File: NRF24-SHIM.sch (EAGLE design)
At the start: 15 parts, among them M1 WIRELESS-NRF24L01, M2 WIRELESS-NRF24L01-PA-EXT

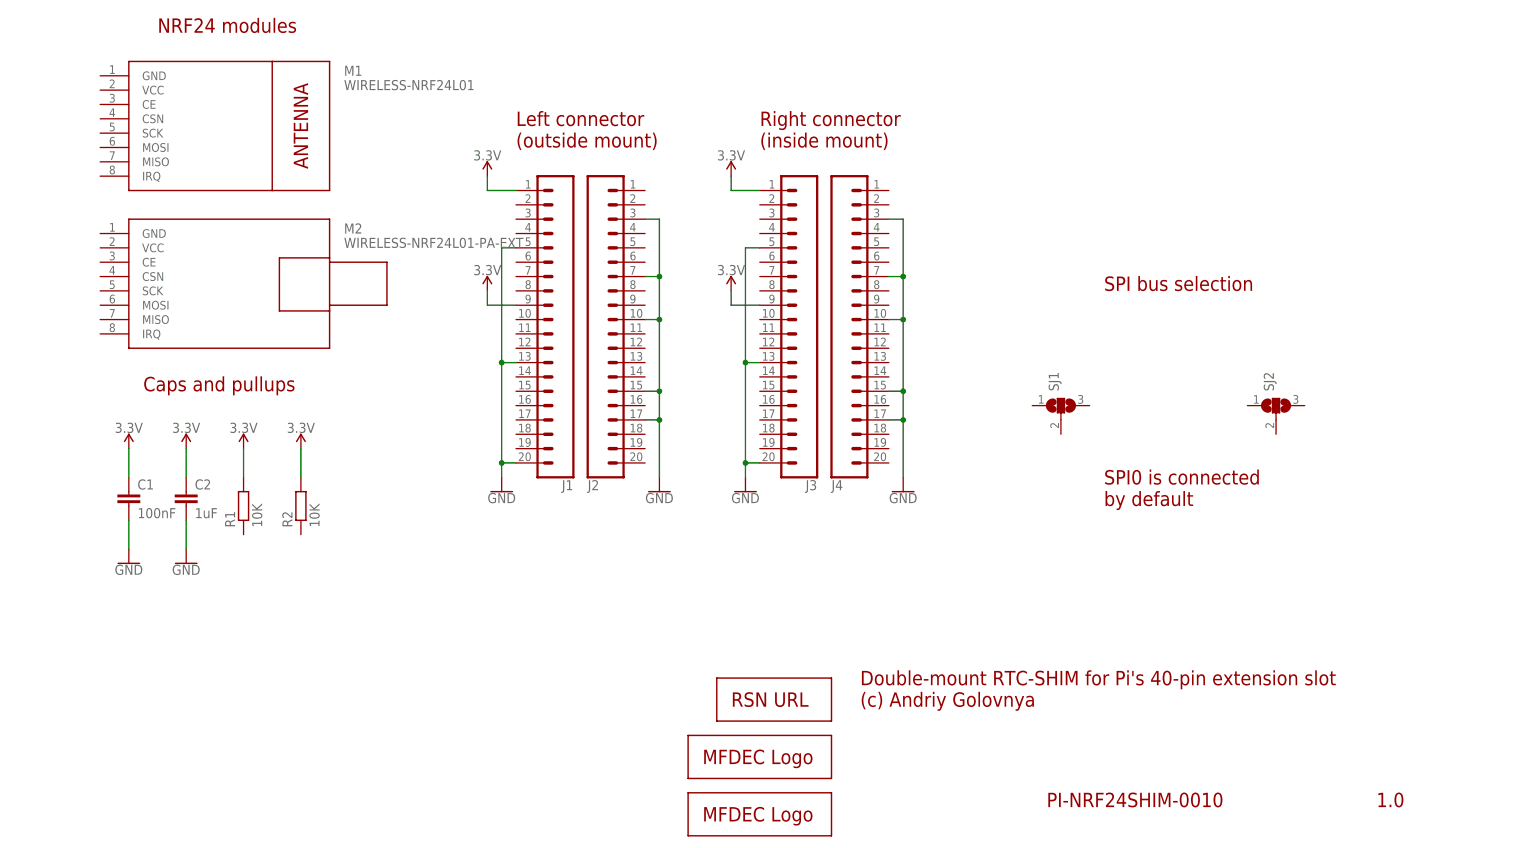
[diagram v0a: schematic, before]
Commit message: Add more pullups. Add more solder joints. Did some tracing.
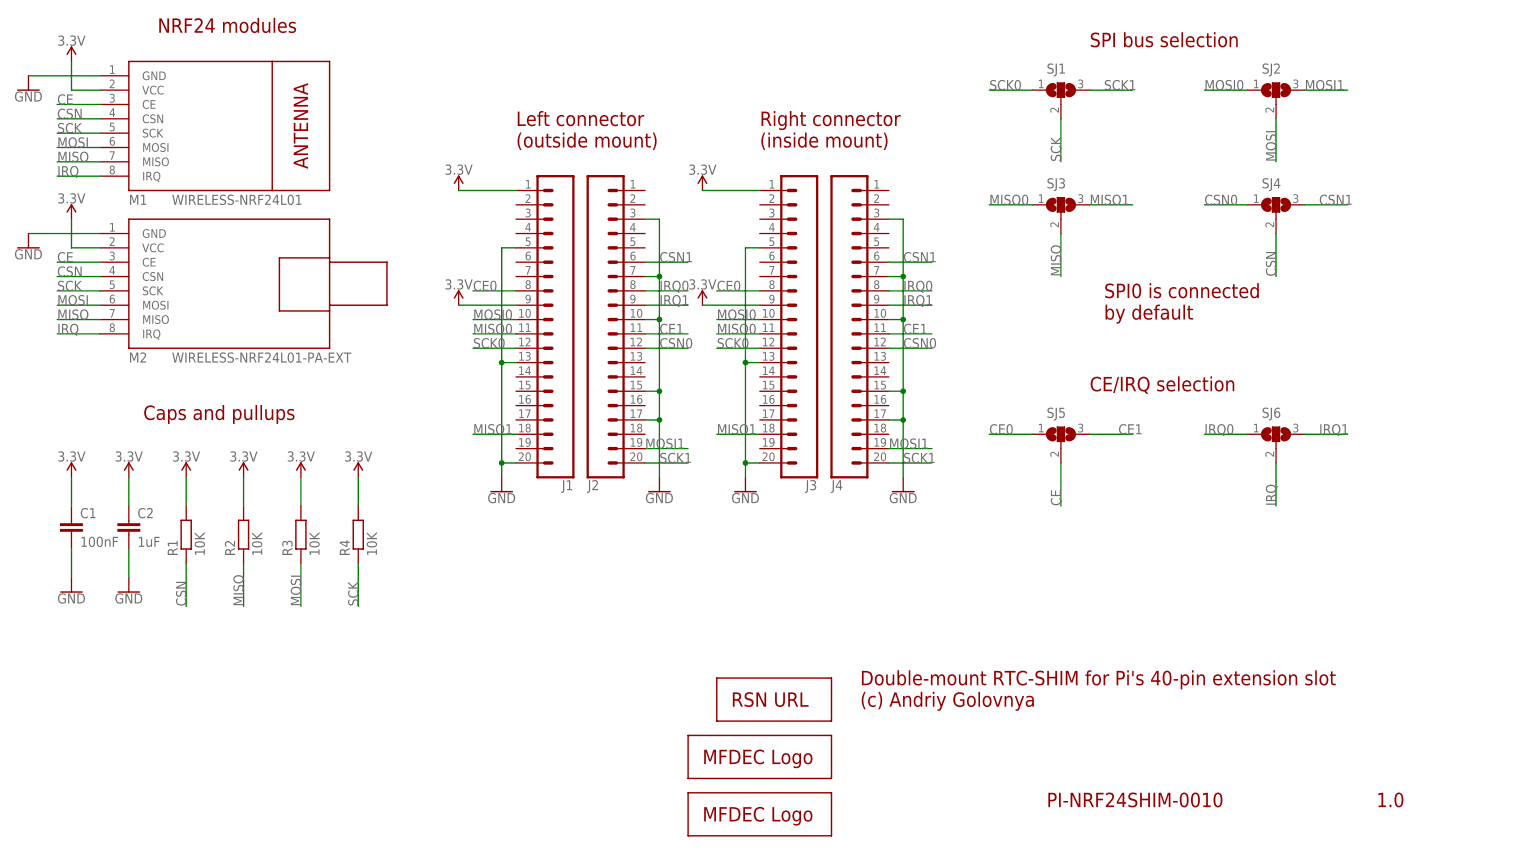
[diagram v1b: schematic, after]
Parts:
- added R3, R4: 10K, rcl:R-EU_R0402
- added SJ3, SJ4, SJ5, SJ6: (no value), _my_jumpers:SJ2
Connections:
- new net CE: M1.CE, M2.CE, SJ5.2
- new net CE0: J1.8, J3.8, SJ5.1
- new net CE1: J2.11, J4.11, SJ5.3
- new net CSN: M1.CSN, M2.CSN, R1.1, SJ4.2
- new net CSN0: J2.12, J4.12, SJ4.1
- new net CSN1: J2.6, J4.6, SJ4.3
- new net IRQ: M1.IRQ, M2.IRQ, SJ6.2
- new net IRQ0: J2.8, J4.8, SJ6.1
- new net IRQ1: J2.9, J4.9, SJ6.3
- new net MISO: M1.MISO, M2.MISO, R2.1, SJ3.2
- new net MISO0: J1.11, J3.11, SJ3.1
- new net MISO1: J1.18, J3.18, SJ3.3
- new net MOSI: M1.MOSI, M2.MOSI, R3.1, SJ2.2
- new net MOSI0: J1.10, J3.10, SJ2.1
- new net MOSI1: J2.19, J4.19, SJ2.3
- new net SCK: M1.SCK, M2.SCK, R4.1, SJ1.2
- new net SCK0: J1.12, J3.12, SJ1.1
- new net SCK1: J2.20, J4.20, SJ1.3
- net 3.3V: now also M1.VCC, M2.VCC, R3.2, R4.2
- net GND: now also M1.GND, M2.GND
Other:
- note added: "CE/IRQ selection"
- moved on the sheet: C1, C2, R1, R2, SJ1, SJ2

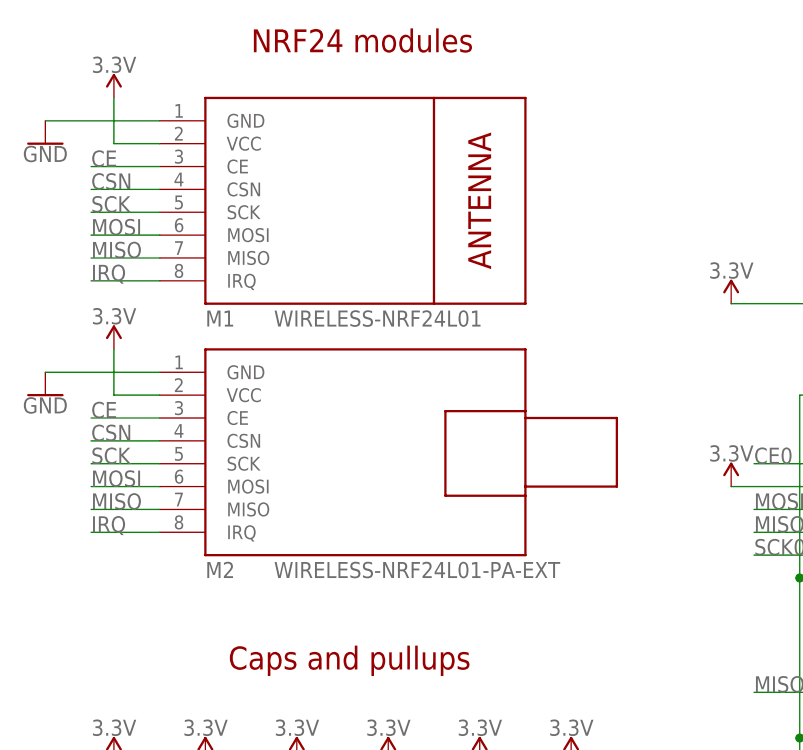
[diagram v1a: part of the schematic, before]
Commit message: Changed NRF24 connector to locked one. Moved passive components closer to the NRF24 connector. Add descriptive texts. Moved some stuff around.
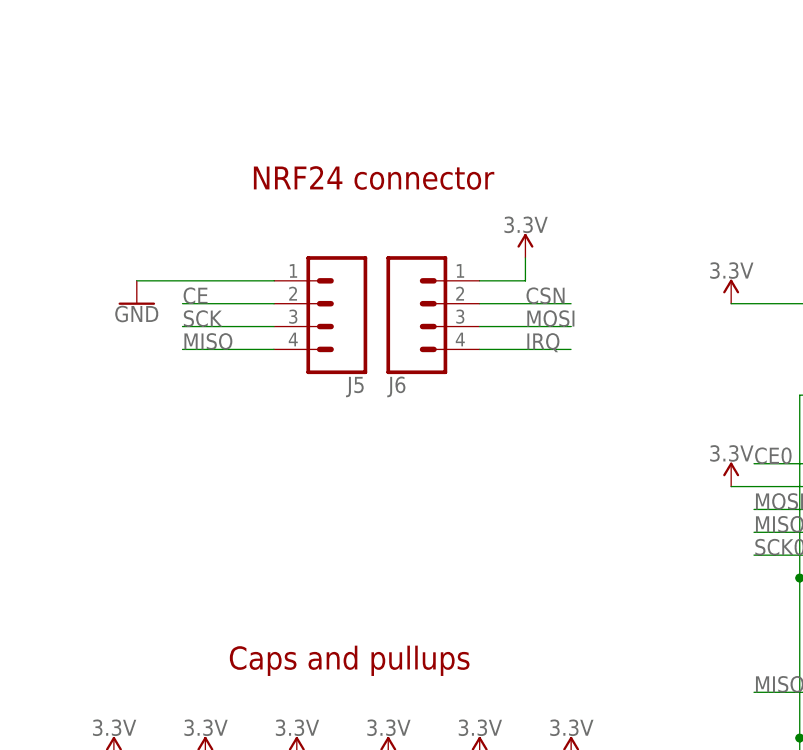
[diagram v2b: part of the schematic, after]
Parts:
- removed M1: WIRELESS-NRF24L01, diy-modules:WIRELESS-NRF24L01
- removed M2: WIRELESS-NRF24L01-PA-EXT, diy-modules:WIRELESS-NRF24L01-PA-EXT
- added J5, J6: (no value), SparkFun-Connectors:CONN_04LOCK
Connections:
- net 3.3V: now also J6.1; no longer M1.VCC, M2.VCC
- net CE: now also J5.2; no longer M1.CE, M2.CE
- net CSN: now also J6.2; no longer M1.CSN, M2.CSN
- net GND: now also J5.1; no longer M1.GND, M2.GND
- net IRQ: now also J6.4; no longer M1.IRQ, M2.IRQ
- net MISO: now also J5.4; no longer M1.MISO, M2.MISO
- net MOSI: now also J6.3; no longer M1.MOSI, M2.MOSI
- net SCK: now also J5.3; no longer M1.SCK, M2.SCK
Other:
- note added: "NRF24 connector"
- note removed: "NRF24 modules"
